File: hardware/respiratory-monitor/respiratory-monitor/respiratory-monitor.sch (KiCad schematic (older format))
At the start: 0 parts

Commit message: Add the basic components
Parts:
- added J?: SFM3xxx_Conn_06_Male, symbol Connector:Conn_01x06_Male
- added U?: ESP32-WROOM-32, RF_Module:ESP32-WROOM-32, symbol RF_Module:ESP32-WROOM-32
- added U?: TCA9509DGKR, DGK8, symbol proj-components:TCA9509DGKR
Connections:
- new net: J?.3 (Pin_3), U?.7 (SCLB)
- new net: J?.5 (Pin_5), U?.6 (SDAB)
- new net +5V: J?.2 (Pin_2), J?.6 (Pin_6), U?.8 (VCCB)
- new net GND: J?.1 (Pin_1), J?.4 (Pin_4), U?.1 (GND), U?.15 (GND), U?.38 (GND), U?.39 (GND), U?.4 (GND)
- new net VCC: U?.1 (VCCA), U?.2 (VDD)
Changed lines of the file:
@@
 Comment4 "Open Source Hardware and Firmware"
 $EndDescr
+$Comp
+L RF_Module:ESP32-WROOM-32 U?
+U 1 1 5E94B77D
+P 1750 2450
+F 0 "U?" H 1300 3800 50  0000 C CNN
+F 1 "ESP32-WROOM-32" H 2200 3800 50  0000 C CNN
+F 2 "RF_Module:ESP32-WROOM-32" H 1750 950 50  0001 C CNN
+F 3 "https://www.espressif.com/sites/default/files/documentation/esp32-wroom-32_datasheet_en.pdf" H 1450 2500 50  0001 C CNN
+	1    1750 2450
+	1    0    0    -1
+$EndComp
+$Comp
+L proj-components:TCA9509DGKR U?
+U 1 1 5E950A6B
+P 3250 1350
+F 0 "U?" H 4450 1737 60  0000 C CNN
+F 1 "TCA9509DGKR" H 4450 1631 60  0000 C CNN
+F 2 "DGK8" H 4450 1590 60  0001 C CNN
+F 3 "" H 3250 1350 60  0000 C CNN
+	1    3250 1350
+	1    0    0    -1
+$EndComp
+$Comp
+L power:GND #PWR?
+U 1 1 5E951891
+P 1750 3850
+F 0 "#PWR?" H 1750 3600 50  0001 C CNN
+F 1 "GND" H 1755 3677 50  0000 C CNN
+F 2 "" H 1750 3850 50  0001 C CNN
+F 3 "" H 1750 3850 50  0001 C CNN
+	1    1750 3850
+	1    0    0    -1
+$EndComp
+$Comp
+L power:VCC #PWR?
+U 1 1 5E951ECF
+P 1750 1050
+F 0 "#PWR?" H 1750 900 50  0001 C CNN
+F 1 "VCC" H 1767 1223 50  0000 C CNN
+F 2 "" H 1750 1050 50  0001 C CNN
+F 3 "" H 1750 1050 50  0001 C CNN
+	1    1750 1050
+	1    0    0    -1
+$EndComp
+$Comp
+L power:GND #PWR?
+U 1 1 5E955F09
+P 3250 1650
+F 0 "#PWR?" H 3250 1400 50  0001 C CNN
+F 1 "GND" H 3255 1477 50  0000 C CNN
+F 2 "" H 3250 1650 50  0001 C CNN
+F 3 "" H 3250 1650 50  0001 C CNN
+	1    3250 1650
+	1    0    0    -1
+$EndComp
+$Comp
+L power:VCC #PWR?
+U 1 1 5E956819
+P 3250 1350
+F 0 "#PWR?" H 3250 1200 50  0001 C CNN
+F 1 "VCC" H 3267 1523 50  0000 C CNN
+F 2 "" H 3250 1350 50  0001 C CNN
+F 3 "" H 3250 1350 50  0001 C CNN
+	1    3250 1350
+	1    0    0    -1
+$EndComp
+$Comp
+L power:GND #PWR?
+U 1 1 5E958A2D
+P 6350 1450
+F 0 "#PWR?" H 6350 1200 50  0001 C CNN
+F 1 "GND" V 6355 1322 50  0000 R CNN
+F 2 "" H 6350 1450 50  0001 C CNN
+F 3 "" H 6350 1450 50  0001 C CNN
+	1    6350 1450
+	0    -1   -1   0
+$EndComp
+$Comp
+L power:+5V #PWR?
+U 1 1 5E95987C
+P 6350 1250
+F 0 "#PWR?" H 6350 1100 50  0001 C CNN
+F 1 "+5V" V 6365 1378 50  0000 L CNN
+F 2 "" H 6350 1250 50  0001 C CNN
+F 3 "" H 6350 1250 50  0001 C CNN
+	1    6350 1250
+	0    1    1    0
+$EndComp
+$Comp
+L power:+5V #PWR?
+U 1 1 5E95A00A
+P 6350 1650
+F 0 "#PWR?" H 6350 1500 50  0001 C CNN
+F 1 "+5V" V 6365 1778 50  0000 L CNN
+F 2 "" H 6350 1650 50  0001 C CNN
+F 3 "" H 6350 1650 50  0001 C CNN
+	1    6350 1650
+	0    1    1    0
+$EndComp
+$Comp
+L power:GND #PWR?
+U 1 1 5E95A62D
+P 6350 1150
+F 0 "#PWR?" H 6350 900 50  0001 C CNN
+F 1 "GND" V 6355 1022 50  0000 R CNN
+F 2 "" H 6350 1150 50  0001 C CNN
+F 3 "" H 6350 1150 50  0001 C CNN
+	1    6350 1150
+	0    -1   -1   0
+$EndComp
+$Comp
+L power:+5V #PWR?
+U 1 1 5E95A820
+P 5650 1350
+F 0 "#PWR?" H 5650 1200 50  0001 C CNN
+F 1 "+5V" V 5665 1478 50  0000 L CNN
+F 2 "" H 5650 1350 50  0001 C CNN
+F 3 "" H 5650 1350 50  0001 C CNN
+	1    5650 1350
+	0    1    1    0
+$EndComp
+$Comp
+L Connector:Conn_01x06_Male J?
+U 1 1 5E94E61D
+P 6150 1350
+F 0 "J?" H 6450 1650 50  0000 C CNN
+F 1 "SFM3xxx_Conn_06_Male" H 5900 1650 50  0000 C CNN
+F 2 "" H 6150 1350 50  0001 C CNN
+F 3 "https://media.digikey.com/pdf/Data%20Sheets/Sensirion%20PDFs/Sensirion_Mass_Flow_Meters_SFM3300_Datasheet.pdf" H 6150 1350 50  0001 C CNN
+	1    6150 1350
+	1    0    0    -1
+$EndComp
+Wire Wire Line
+	5650 1550 6350 1550
+Wire Wire Line
+	5650 1450 6000 1450
+Wire Wire Line
+	6000 1450 6000 1350
+Wire Wire Line
+	6000 1350 6350 1350
 $EndSCHEMATC

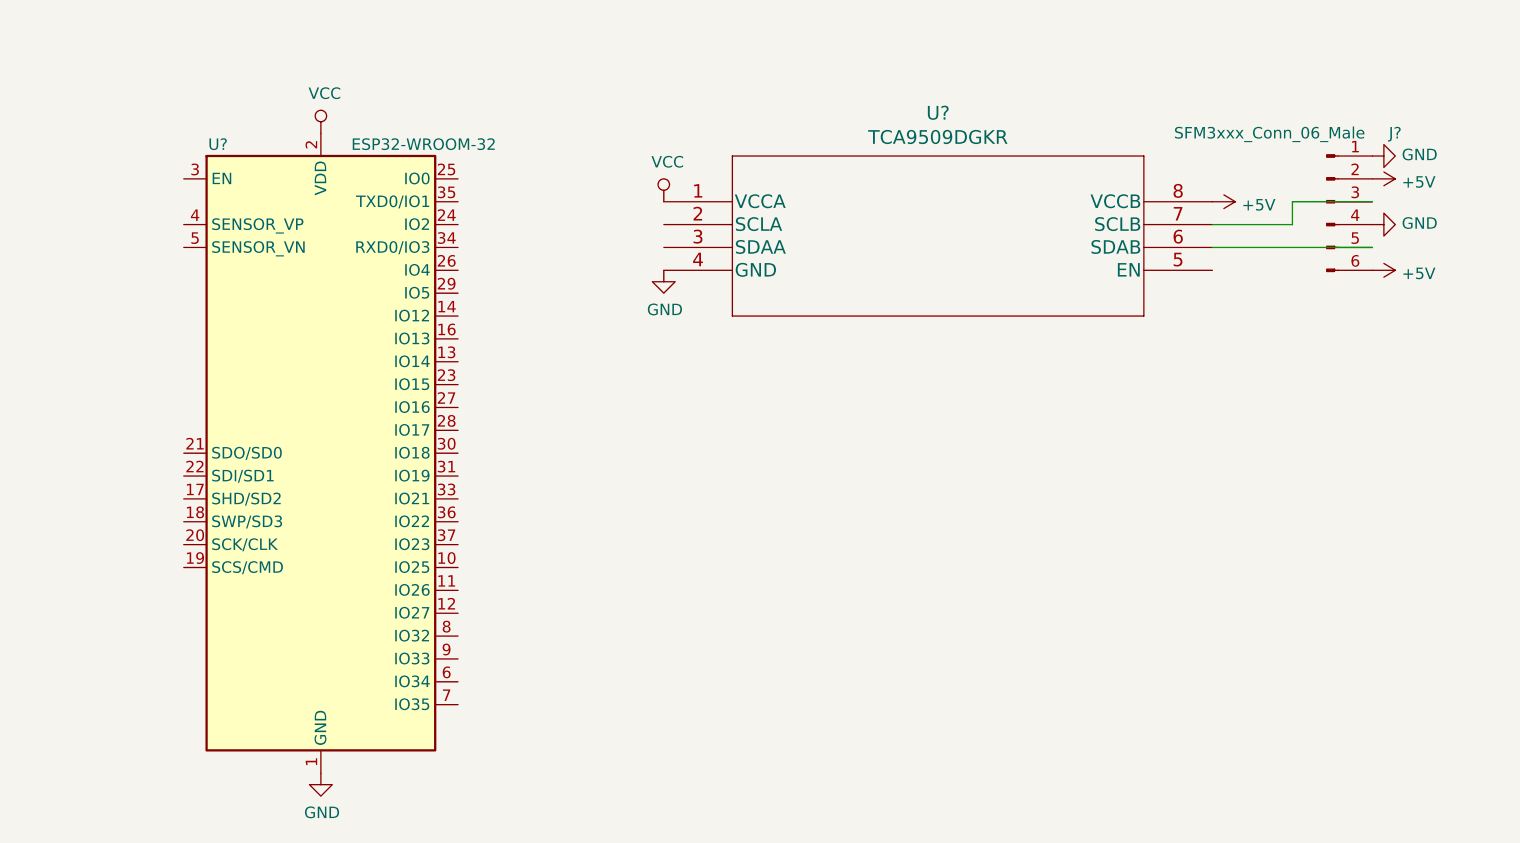
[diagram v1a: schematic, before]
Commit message: Add bypass caps
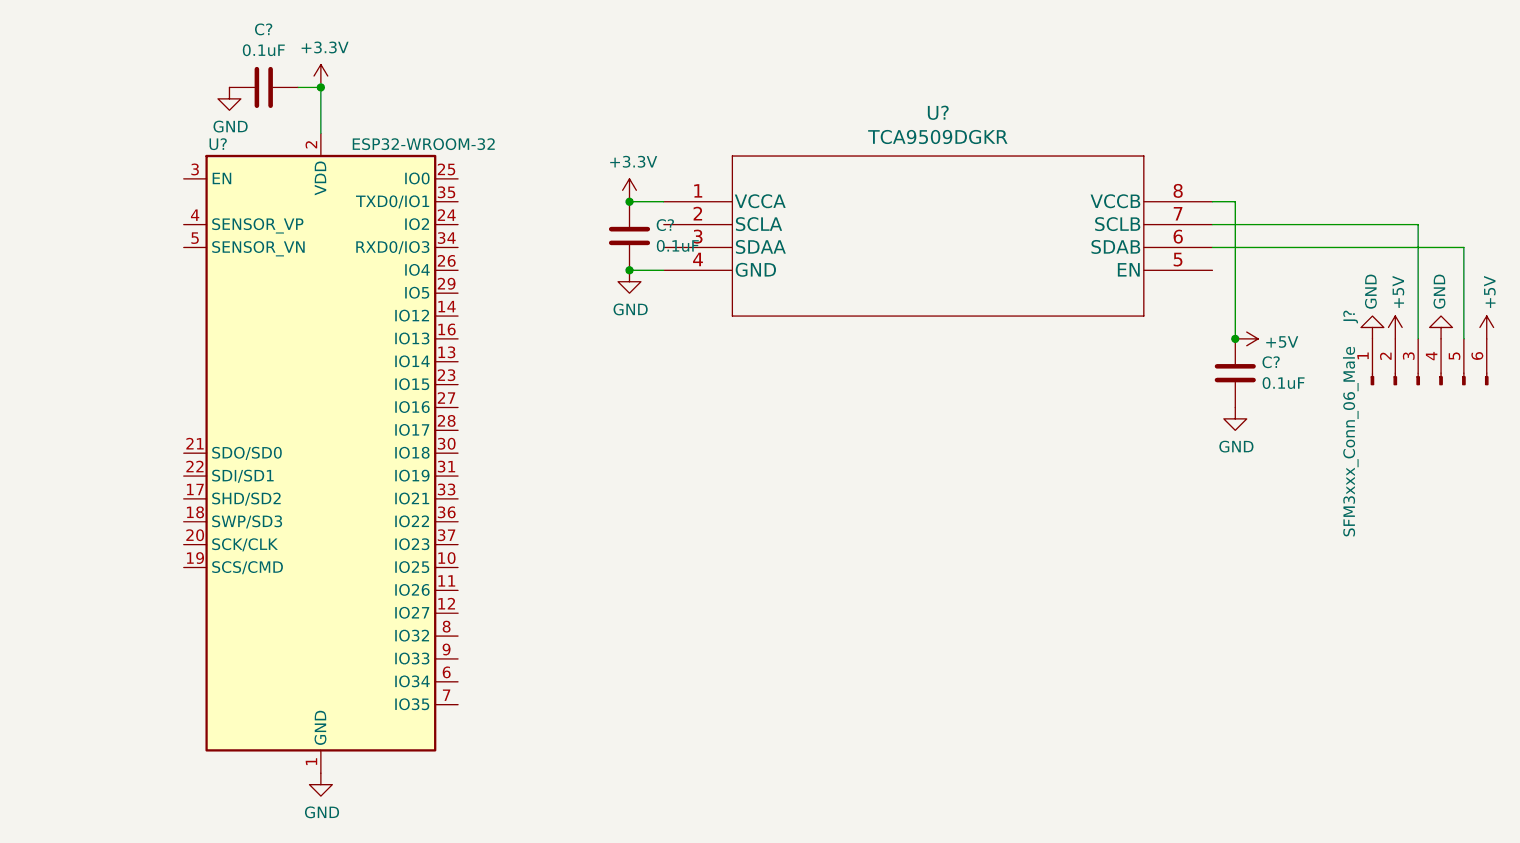
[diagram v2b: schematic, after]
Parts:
- added C? (x3): 0.1uF, symbol Device:C
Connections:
- net +5V: now also C?.1
- net GND: now also C?.2, C?.2, C?.2
- net VCC renamed +3V3
- net +3V3: now also C?.1, C?.1
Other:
- moved on the sheet: J?
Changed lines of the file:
@@
-$EndComp
-$Comp
-L power:VCC #PWR?
-U 1 1 5E951ECF
-P 1750 1050
-F 0 "#PWR?" H 1750 900 50  0001 C CNN
-F 1 "VCC" H 1767 1223 50  0000 C CNN
-F 2 "" H 1750 1050 50  0001 C CNN
-F 3 "" H 1750 1050 50  0001 C CNN
-	1    1750 1050
-	1    0    0    -1
 $EndComp
 $Comp
 L power:GND #PWR?
 U 1 1 5E955F09
-P 3250 1650
-F 0 "#PWR?" H 3250 1400 50  0001 C CNN
-F 1 "GND" H 3255 1477 50  0000 C CNN
-F 2 "" H 3250 1650 50  0001 C CNN
-F 3 "" H 3250 1650 50  0001 C CNN
-	1    3250 1650
-	1    0    0    -1
-$EndComp
-$Comp
-L power:VCC #PWR?
-U 1 1 5E956819
-P 3250 1350
-F 0 "#PWR?" H 3250 1200 50  0001 C CNN
-F 1 "VCC" H 3267 1523 50  0000 C CNN
-F 2 "" H 3250 1350 50  0001 C CNN
-F 3 "" H 3250 1350 50  0001 C CNN
-	1    3250 1350
+P 3100 1650
+F 0 "#PWR?" H 3100 1400 50  0001 C CNN
+F 1 "GND" H 3105 1477 50  0000 C CNN
+F 2 "" H 3100 1650 50  0001 C CNN
+F 3 "" H 3100 1650 50  0001 C CNN
+	1    3100 1650
 	1    0    0    -1
 $EndComp
@@
 L power:GND #PWR?
 U 1 1 5E958A2D
-P 6350 1450
-F 0 "#PWR?" H 6350 1200 50  0001 C CNN
-F 1 "GND" V 6355 1322 50  0000 R CNN
-F 2 "" H 6350 1450 50  0001 C CNN
-F 3 "" H 6350 1450 50  0001 C CNN
-	1    6350 1450
-	0    -1   -1   0
+P 6650 1950
+F 0 "#PWR?" H 6650 1700 50  0001 C CNN
+F 1 "GND" V 6655 1822 50  0000 R CNN
+F 2 "" H 6650 1950 50  0001 C CNN
+F 3 "" H 6650 1950 50  0001 C CNN
+	1    6650 1950
+	-1   0    0    1
 $EndComp
 $Comp
 L power:+5V #PWR?
 U 1 1 5E95987C
-P 6350 1250
-F 0 "#PWR?" H 6350 1100 50  0001 C CNN
-F 1 "+5V" V 6365 1378 50  0000 L CNN
-F 2 "" H 6350 1250 50  0001 C CNN
-F 3 "" H 6350 1250 50  0001 C CNN
-	1    6350 1250
-	0    1    1    0
+P 6450 1950
+F 0 "#PWR?" H 6450 1800 50  0001 C CNN
+F 1 "+5V" V 6465 2078 50  0000 L CNN
+F 2 "" H 6450 1950 50  0001 C CNN
+F 3 "" H 6450 1950 50  0001 C CNN
+	1    6450 1950
+	1    0    0    -1
 $EndComp
 $Comp
 L power:+5V #PWR?
 U 1 1 5E95A00A
-P 6350 1650
-F 0 "#PWR?" H 6350 1500 50  0001 C CNN
-F 1 "+5V" V 6365 1778 50  0000 L CNN
-F 2 "" H 6350 1650 50  0001 C CNN
-F 3 "" H 6350 1650 50  0001 C CNN
-	1    6350 1650
-	0    1    1    0
+P 6850 1950
+F 0 "#PWR?" H 6850 1800 50  0001 C CNN
+F 1 "+5V" V 6865 2078 50  0000 L CNN
+F 2 "" H 6850 1950 50  0001 C CNN
+F 3 "" H 6850 1950 50  0001 C CNN
+	1    6850 1950
+	1    0    0    -1
 $EndComp
 $Comp
 L power:GND #PWR?
 U 1 1 5E95A62D
-P 6350 1150
-F 0 "#PWR?" H 6350 900 50  0001 C CNN
-F 1 "GND" V 6355 1022 50  0000 R CNN
-F 2 "" H 6350 1150 50  0001 C CNN
-F 3 "" H 6350 1150 50  0001 C CNN
-	1    6350 1150
-	0    -1   -1   0
+P 6350 1950
+F 0 "#PWR?" H 6350 1700 50  0001 C CNN
+F 1 "GND" V 6355 1822 50  0000 R CNN
+F 2 "" H 6350 1950 50  0001 C CNN
+F 3 "" H 6350 1950 50  0001 C CNN
+	1    6350 1950
+	-1   0    0    1
 $EndComp
 $Comp
 L power:+5V #PWR?
 U 1 1 5E95A820
-P 5650 1350
-F 0 "#PWR?" H 5650 1200 50  0001 C CNN
-F 1 "+5V" V 5665 1478 50  0000 L CNN
-F 2 "" H 5650 1350 50  0001 C CNN
-F 3 "" H 5650 1350 50  0001 C CNN
-	1    5650 1350
+P 5750 1950
+F 0 "#PWR?" H 5750 1800 50  0001 C CNN
+F 1 "+5V" V 5765 2078 50  0000 L CNN
+F 2 "" H 5750 1950 50  0001 C CNN
+F 3 "" H 5750 1950 50  0001 C CNN
+	1    5750 1950
 	0    1    1    0
 $EndComp
@@
 L Connector:Conn_01x06_Male J?
 U 1 1 5E94E61D
-P 6150 1350
-F 0 "J?" H 6450 1650 50  0000 C CNN
-F 1 "SFM3xxx_Conn_06_Male" H 5900 1650 50  0000 C CNN
-F 2 "" H 6150 1350 50  0001 C CNN
-F 3 "https://media.digikey.com/pdf/Data%20Sheets/Sensirion%20PDFs/Sensirion_Mass_Flow_Meters_SFM3300_Datasheet.pdf" H 6150 1350 50  0001 C CNN
-	1    6150 1350
+P 6550 2150
+F 0 "J?" H 6850 2450 50  0000 C CNN
+F 1 "SFM3xxx_Conn_06_Male" H 6300 2450 50  0000 C CNN
+F 2 "" H 6550 2150 50  0001 C CNN
+F 3 "https://media.digikey.com/pdf/Data%20Sheets/Sensirion%20PDFs/Sensirion_Mass_Flow_Meters_SFM3300_Datasheet.pdf" H 6550 2150 50  0001 C CNN
+	1    6550 2150
+	0    -1   -1   0
+$EndComp
+Wire Wire Line
+	3100 1650 3250 1650
+Wire Wire Line
+	3250 1350 3100 1350
+$Comp
+L Device:C C?
+U 1 1 5E96635E
+P 3100 1500
+F 0 "C?" H 3215 1546 50  0000 L CNN
+F 1 "0.1uF" H 3215 1455 50  0000 L CNN
+F 2 "" H 3138 1350 50  0001 C CNN
+F 3 "~" H 3100 1500 50  0001 C CNN
+	1    3100 1500
+	1    0    0    -1
+$EndComp
+Connection ~ 3100 1650
+$Comp
+L Device:C C?
+U 1 1 5E966B53
+P 5750 2100
+F 0 "C?" H 5865 2146 50  0000 L CNN
+F 1 "0.1uF" H 5865 2055 50  0000 L CNN
+F 2 "" H 5788 1950 50  0001 C CNN
+F 3 "~" H 5750 2100 50  0001 C CNN
+	1    5750 2100
+	1    0    0    -1
+$EndComp
+$Comp
+L power:GND #PWR?
+U 1 1 5E9671DA
+P 5750 2250
+F 0 "#PWR?" H 5750 2000 50  0001 C CNN
+F 1 "GND" H 5755 2077 50  0000 C CNN
+F 2 "" H 5750 2250 50  0001 C CNN
+F 3 "" H 5750 2250 50  0001 C CNN
+	1    5750 2250
 	1    0    0    -1
 $EndComp
 Wire Wire Line
-	5650 1550 6350 1550
+	5750 1950 5750 1350
 Wire Wire Line
-	5650 1450 6000 1450
+	5750 1350 5650 1350
+Connection ~ 5750 1950
 Wire Wire Line
-	6000 1450 6000 1350
+	6550 1950 6550 1450
 Wire Wire Line
-	6000 1350 6350 1350
+	6550 1450 5650 1450
+Wire Wire Line
+	5650 1550 6750 1550
+Wire Wire Line
+	6750 1550 6750 1950
+$Comp
+L power:GND #PWR?
+U 1 1 5E972038
+P 1350 850
+F 0 "#PWR?" H 1350 600 50  0001 C CNN
+F 1 "GND" H 1355 677 50  0000 C CNN
+F 2 "" H 1350 850 50  0001 C CNN
+F 3 "" H 1350 850 50  0001 C CNN
+	1    1350 850
+	1    0    0    -1
+$EndComp
+$Comp
+L Device:C C?
+U 1 1 5E9726C9
+P 1500 850
+F 0 "C?" V 1248 850 50  0000 C CNN
+F 1 "0.1uF" V 1339 850 50  0000 C CNN
+F 2 "" H 1538 700 50  0001 C CNN
+F 3 "~" H 1500 850 50  0001 C CNN
+	1    1500 850
+	0    1    1    0
+$EndComp
+Wire Wire Line
+	1750 850  1750 1050
+$Comp
+L power:+3.3V #PWR?
+U 1 1 5E973DA6
+P 1750 850
+F 0 "#PWR?" H 1750 700 50  0001 C CNN
+F 1 "+3.3V" H 1765 1023 50  0000 C CNN
+F 2 "" H 1750 850 50  0001 C CNN
+F 3 "" H 1750 850 50  0001 C CNN
+	1    1750 850
+	1    0    0    -1
+$EndComp
+$Comp
+L power:+3.3V #PWR?
+U 1 1 5E97487C
+P 3100 1350
+F 0 "#PWR?" H 3100 1200 50  0001 C CNN
+F 1 "+3.3V" H 3115 1523 50  0000 C CNN
+F 2 "" H 3100 1350 50  0001 C CNN
+F 3 "" H 3100 1350 50  0001 C CNN
+	1    3100 1350
+	1    0    0    -1
+$EndComp
+Connection ~ 3100 1350
+Wire Wire Line
+	1650 850  1750 850
+Connection ~ 1750 850
 $EndSCHEMATC

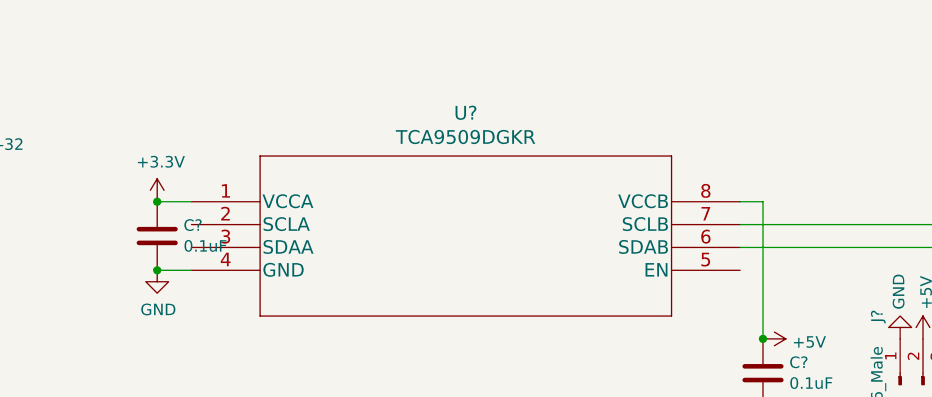
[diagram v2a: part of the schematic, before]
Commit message: Add digikey link and part number
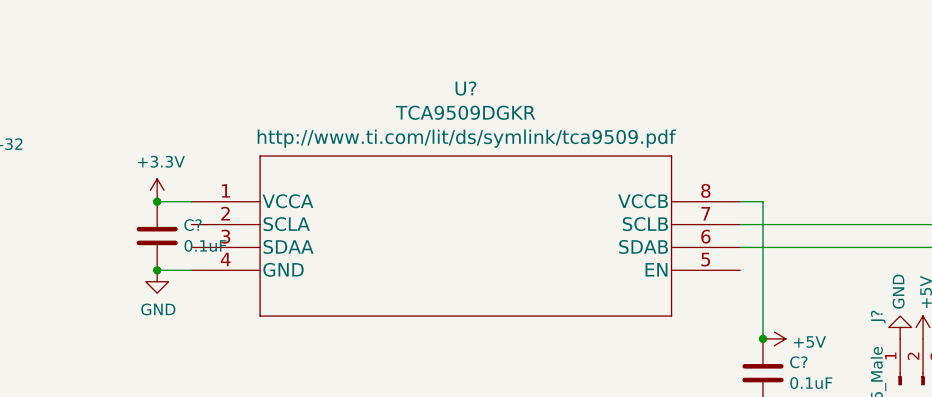
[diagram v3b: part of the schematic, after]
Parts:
- U?: DigiKey (none) -> https://www.digikey.com/product-detail/en/espressif-systems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; DigiKeyPartNumber (none) -> 1904-1010-1-ND
- U?: DigiKey (none) -> https://www.digikey.com/product-detail/en/texas-instruments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; DigiKeyPartNumber (none) -> 296-30283-1-ND
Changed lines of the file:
@@
 F 2 "RF_Module:ESP32-WROOM-32" H 1750 950 50  0001 C CNN
 F 3 "https://www.espressif.com/sites/default/files/documentation/esp32-wroom-32_datasheet_en.pdf" H 1450 2500 50  0001 C CNN
+F 4 "https://www.digikey.com/product-detail/en/espressif-systems/ESP32-WROOM-32/1904-1010-1-ND/8544305" H 1750 2450 50  0001 C CNN "DigiKey"
+F 5 "1904-1010-1-ND" H 1750 2450 50  0001 C CNN "DigiKeyPartNumber"
 	1    1750 2450
 	1    0    0    -1
@@
 U 1 1 5E950A6B
 P 3250 1350
-F 0 "U?" H 4450 1737 60  0000 C CNN
-F 1 "TCA9509DGKR" H 4450 1631 60  0000 C CNN
+F 0 "U?" H 4450 1843 60  0000 C CNN
+F 1 "TCA9509DGKR" H 4450 1737 60  0000 C CNN
 F 2 "DGK8" H 4450 1590 60  0001 C CNN
-F 3 "" H 3250 1350 60  0000 C CNN
+F 3 "http://www.ti.com/lit/ds/symlink/tca9509.pdf" H 4450 1631 60  0000 C CNN
+F 4 "https://www.digikey.com/product-detail/en/texas-instruments/TCA9509DGKR/296-30283-1-ND/3060760" H 3250 1350 50  0001 C CNN "DigiKey"
+F 5 "296-30283-1-ND" H 3250 1350 50  0001 C CNN "DigiKeyPartNumber"
 	1    3250 1350
 	1    0    0    -1
